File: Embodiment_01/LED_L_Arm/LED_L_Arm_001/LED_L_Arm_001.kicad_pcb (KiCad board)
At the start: 2 copper layers, 14 parts, among them J1 Conn_01x01_Female, J2 Conn_01x01_Female

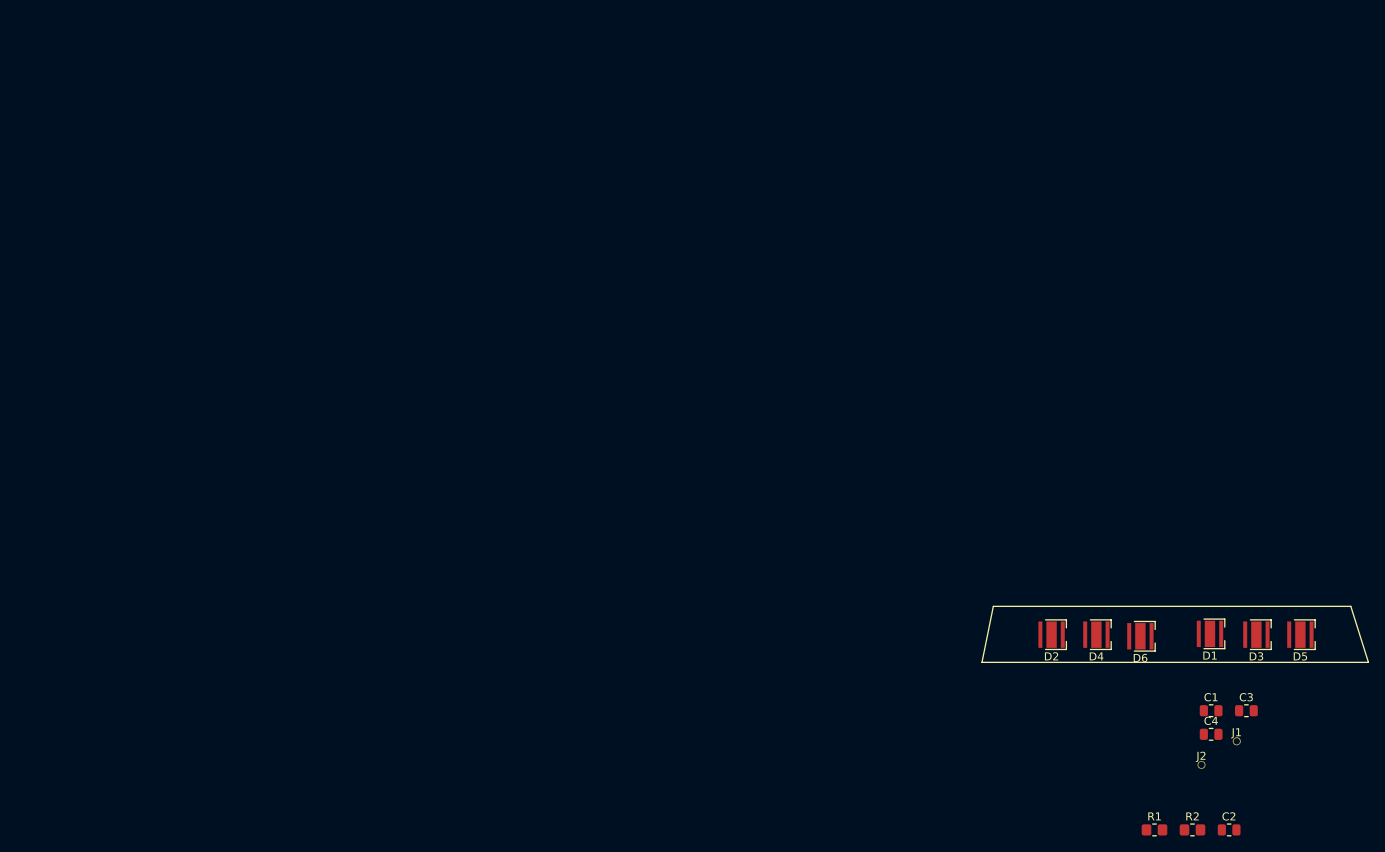
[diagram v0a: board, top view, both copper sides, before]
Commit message: Calculation of shape, PCB
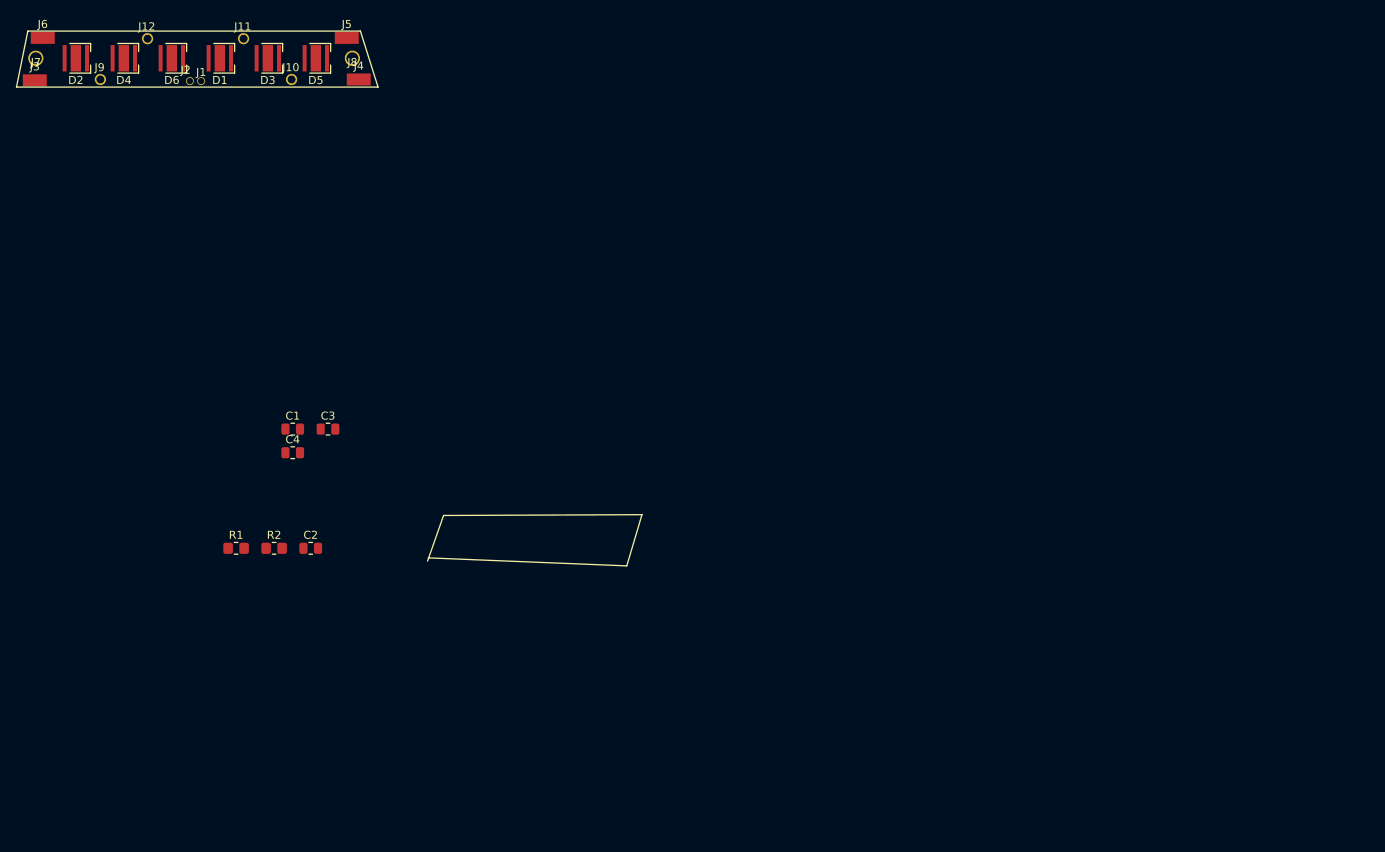
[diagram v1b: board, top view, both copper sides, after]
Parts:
- added J10: Conn_01x01_Female, pins:pin_1.0, F.Cu at (34.4, 7.70)
- added J11: Conn_01x01_Female, pins:pin_1.0, F.Cu at (28.4, 2.60)
- added J12: Conn_01x01_Female, pins:pin_1.0, F.Cu at (16.4, 2.60)
- added J3: Conn_01x01_Female, pins:WireSidePlate_001, F.Cu at (2.40, 7.60)
- added J4: Conn_01x01_Female, pins:WireSidePlate_001, F.Cu at (42.9, 7.50)
- added J5: Conn_01x01_Female, pins:WireSidePlate_001, F.Cu at (41.4, 2.30)
- added J6: Conn_01x01_Female, pins:WireSidePlate_001, F.Cu at (3.40, 2.30)
- added J7: Conn_01x01_Female, pins:pin_1.5, F.Cu at (2.53, 7.05)
- added J8: Conn_01x01_Female, pins:pin_1.5, F.Cu at (42.1, 7.05)
- added J9: Conn_01x01_Female, pins:pin_1.0, F.Cu at (10.5, 7.70)
- moved J1 153.5 mm to (23.2, 8.30)
- moved J2 152.6 mm to (21.8, 8.30)
- moved D1 143.2 mm to (25.5, 7.05)
- moved D3 143.0 mm to (31.5, 7.05)
- moved D5 142.6 mm to (37.5, 7.05)
- moved D2 141.7 mm to (7.53, 7.05)
- moved D4 141.3 mm to (13.5, 7.05)
- moved D6 141.0 mm to (19.5, 7.05)
- moved R1 120.1 mm to (27.6, 68.3)
- moved R2 120.1 mm to (32.3, 68.3)
- moved C1 120.1 mm to (34.6, 53.4)
- moved C2 120.1 mm to (36.9, 68.3)
- moved C3 120.1 mm to (39.1, 53.4)
- moved C4 120.1 mm to (34.6, 56.4)
